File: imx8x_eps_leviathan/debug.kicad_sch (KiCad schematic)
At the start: 78 parts, among them J11 Conn_01x05_Pin, U19 CAT93C66VI-GT3, U20 FT2232HL, U21 LP38693MP-ADJ/NOPB, U22 TXS0101DCKR, U23 TXS0101DCKR, Y1 12MHz

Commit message: Did stufffffff
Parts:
- C61, C62, C63, C64, C65, C66, C67, C68, C69, C70, C71, C72, C73, C74, C75, C76, C77, C78, C79, C80, C81: footprint (none) -> EPS:C0402
- J11: footprint (none) -> Connector_PinHeader_1.00mm:PinHeader_1x05_P1.00mm_Horizontal
- L4, L5: footprint (none) -> imx8_carrier_board_footprints:L0805
- R102, R103, R104, R105, R106, R107, R108, R109, R110, R111, R112, R113, R114, R115, R116, R117, R118, R119, R120, R121, R122, R123, R124, R125, R126, R127, R128, R129, R130, R131, R132, R133, R134, R135, R136, R137, R138, R139, R140, R141, R142, R143, R144, R145, R146, R147: footprint (none) -> EPS:R0402
- USB1: footprint libs:MICRO-USB-SMD_10118194-0001LF -> imx8_carrier_board_footprints:MICRO-USB-SMD_10118194-0001LF
- Y1: footprint (none) -> imx8_carrier_board_footprints:CRYSTAL-SMD_4P-L3.2-W2.5-BL

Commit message: for john
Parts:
- R103: now not fitted
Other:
- note added: "UART Level Shifters"
- note removed: "UART Level ShifterS"
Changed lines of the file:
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@@
 		)
 	)
-	(text "UART Level ShifterS"
+	(text "UART Level Shifters"
 		(exclude_from_sim no)
 		(at 244.348 95.758 0)
@@
 		(in_bom yes)
 		(on_board yes)
-		(dnp no)
+		(dnp yes)
 		(property "Reference" "R103"
 			(at 45.466 87.376 0)

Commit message: bruh
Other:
- title: Debug USB - UART -> Leviathan 1-A
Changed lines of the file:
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@@
 	(paper "A4")
 	(title_block
-		(title "Debug USB - UART")
+		(title "Leviathan 1-A")
+		(date "2025-10-22")
+		(rev "1-A")
 		(company "Bronco Space Lab")
 		(comment 1 "By John Pollak & Luca Lanzillotta")

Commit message: Updated Schematic and SOM
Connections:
- net VCC_3V3_OUT renamed +3.3V_OBC_Perif
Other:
- note removed: "?"

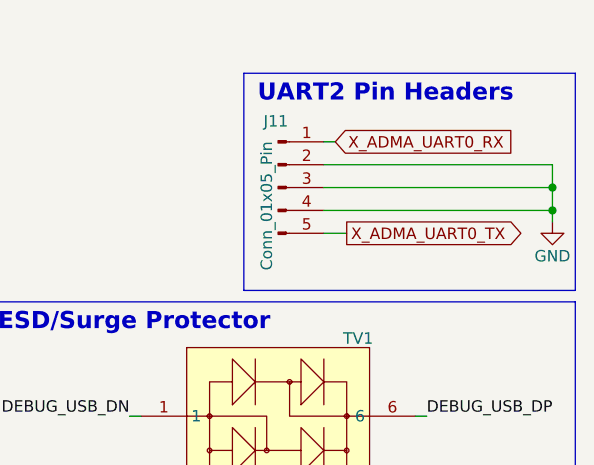
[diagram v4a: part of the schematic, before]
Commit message: Schematic Need Double Checking, But I think its done
I think ive finished adding every change we wanted to include after the merging along with all the changes requested by PHYTEC. I would like to sit down and review the muxing configuration and double check every single sheet to make sure its perfect. then we can send it off to Phytec.
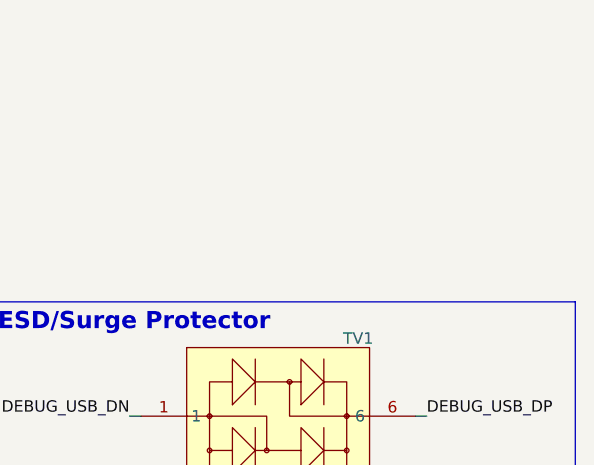
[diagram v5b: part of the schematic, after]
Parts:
- removed J11: Conn_01x05_Pin, Connector_PinHeader_1.00mm:PinHeader_1x05_P1.00mm_Horizontal, symbol Connector:Conn_01x05_Pin
- Y1: LCSC Part (none) -> C9002
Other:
- note removed: "UART2 Pin Headers"

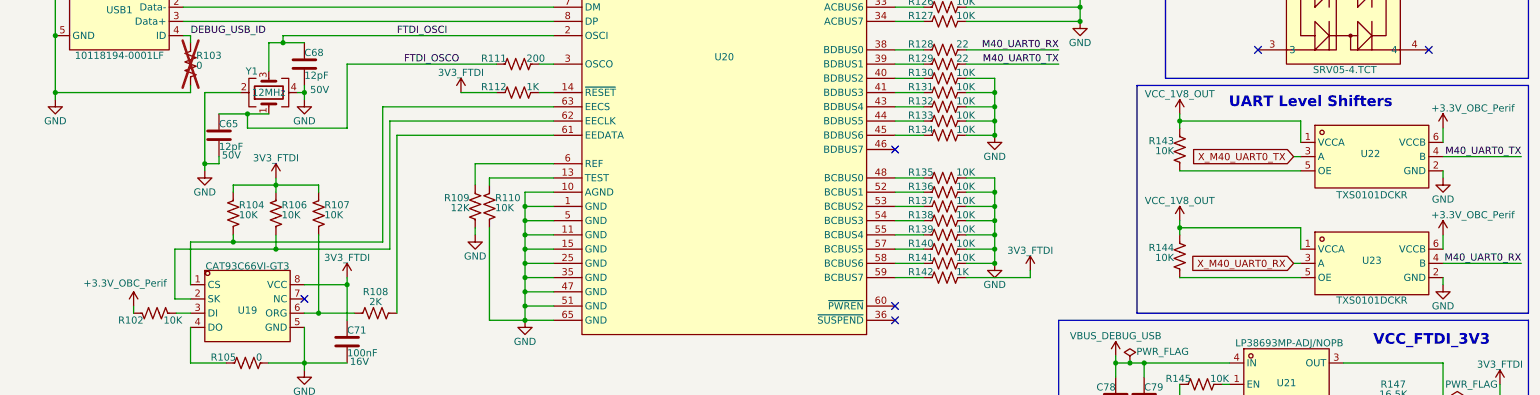
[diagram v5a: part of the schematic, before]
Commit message: Schematic Complete. Ready for Phytec.
Fixed muxing with a few things that were missing with ETH1, and corrected some missing labels. Ready for Phytecs review.
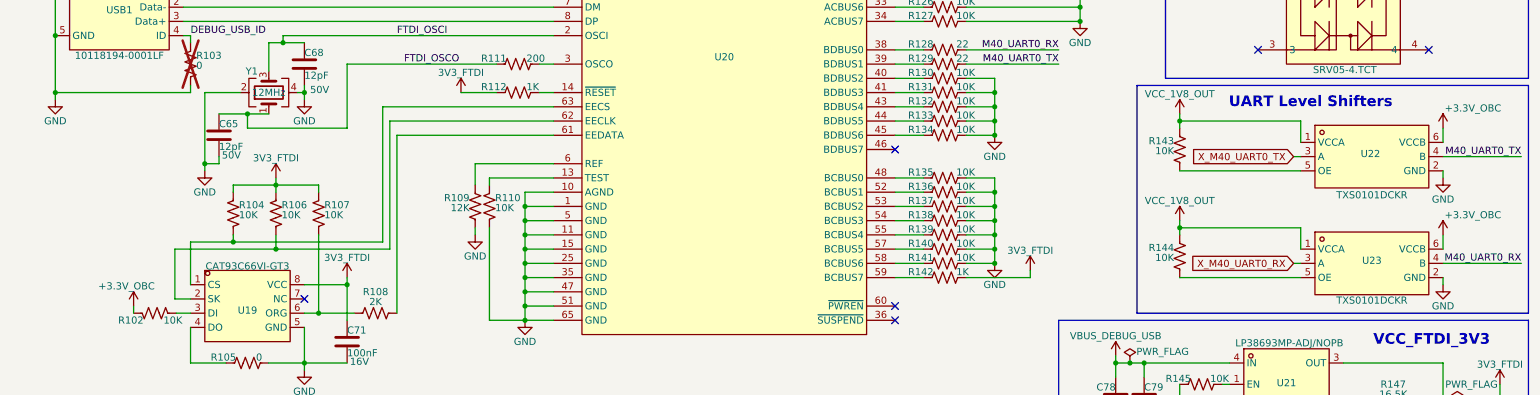
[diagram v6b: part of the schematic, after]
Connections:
- net +3.3V_OBC_Perif renamed +3.3V_OBC
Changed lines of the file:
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@@
 	)
 	(symbol
-		(lib_id "power:+3.3V")
-		(at 267.97 119.38 0)
-		(unit 1)
-		(exclude_from_sim no)
-		(in_bom yes)
-		(on_board yes)
-		(dnp no)
-		(property "Reference" "#PWR0108"
-			(at 267.97 123.19 0)
-			(effects
-				(font
-					(size 1.27 1.27)
-				)
-				(hide yes)
-			)
-		)
-		(property "Value" "+3.3V_OBC_Perif"
-			(at 273.304 115.824 0)
-			(effects
-				(font
-					(size 1.27 1.27)
-				)
-			)
-		)
-		(property "Footprint" ""
-			(at 267.97 119.38 0)
-			(effects
-				(font
-					(size 1.27 1.27)
-				)
-				(hide yes)
-			)
-		)
-		(property "Datasheet" ""
-			(at 267.97 119.38 0)
-			(effects
-				(font
-					(size 1.27 1.27)
-				)
-				(hide yes)
-			)
-		)
-		(property "Description" "Power symbol creates a global label with name \"+3.3V\""
-			(at 267.97 119.38 0)
-			(effects
-				(font
-					(size 1.27 1.27)
-				)
-				(hide yes)
-			)
-		)
-		(pin "1"
-		)
-		(instances
-			(project "imx8x_eps_leviathan"
-				(path "/bd3af9f3-19df-4a2f-8b54-98c48cea082e/1b5b2e76-614d-4307-9232-e06f7c77302d/af0dcf25-e67e-4174-8f3a-a0b953038707"
-					(reference "#PWR0108")
-					(unit 1)
-				)
-			)
-		)
-	)
-	(symbol
 		(lib_id "Device:R_US")
 		(at 179.07 116.84 270)
@@
 	(symbol
 		(lib_id "power:+3.3V")
-		(at 34.29 132.08 0)
+		(at 267.97 100.33 0)
 		(unit 1)
 		(exclude_from_sim no)
@@
 		(on_board yes)
 		(dnp no)
-		(property "Reference" "#PWR069"
-			(at 34.29 135.89 0)
+		(property "Reference" "#PWR0106"
+			(at 267.97 104.14 0)
 			(effects
 				(font
@@
 			)
 		)
-		(property "Value" "+3.3V_OBC_Perif"
-			(at 32.766 128.016 0)
+		(property "Value" "+3.3V_OBC"
+			(at 273.304 96.774 0)
 			(effects
 				(font
@@
 		)
 		(property "Footprint" ""
-			(at 34.29 132.08 0)
+			(at 267.97 100.33 0)
 			(effects
 				(font
@@
 		)
 		(property "Datasheet" ""
-			(at 34.29 132.08 0)
+			(at 267.97 100.33 0)
 			(effects
 				(font
@@
 		)
 		(property "Description" "Power symbol creates a global label with name \"+3.3V\""
-			(at 34.29 132.08 0)
+			(at 267.97 100.33 0)
 			(effects
 				(font
@@
 			(project "imx8x_eps_leviathan"
 				(path "/bd3af9f3-19df-4a2f-8b54-98c48cea082e/1b5b2e76-614d-4307-9232-e06f7c77302d/af0dcf25-e67e-4174-8f3a-a0b953038707"
-					(reference "#PWR069")
+					(reference "#PWR0106")
 					(unit 1)
 				)
@@
 	)
 	(symbol
+		(lib_id "power:+3.3V")
+		(at 34.29 132.08 0)
+		(unit 1)
+		(exclude_from_sim no)
+		(in_bom yes)
+		(on_board yes)
+		(dnp no)
+		(property "Reference" "#PWR069"
+			(at 34.29 135.89 0)
+			(effects
+				(font
+					(size 1.27 1.27)
+				)
+				(hide yes)
+			)
+		)
+		(property "Value" "+3.3V_OBC"
+			(at 33.02 128.524 0)
+			(effects
+				(font
+					(size 1.27 1.27)
+				)
+			)
+		)
+		(property "Footprint" ""
+			(at 34.29 132.08 0)
+			(effects
+				(font
+					(size 1.27 1.27)
+				)
+				(hide yes)
+			)
+		)
+		(property "Datasheet" ""
+			(at 34.29 132.08 0)
+			(effects
+				(font
+					(size 1.27 1.27)
+				)
+				(hide yes)
+			)
+		)
+		(property "Description" "Power symbol creates a global label with name \"+3.3V\""
+			(at 34.29 132.08 0)
+			(effects
+				(font
+					(size 1.27 1.27)
+				)
+				(hide yes)
+			)
+		)
+		(pin "1"
+		)
+		(instances
+			(project "imx8x_eps_leviathan"
+				(path "/bd3af9f3-19df-4a2f-8b54-98c48cea082e/1b5b2e76-614d-4307-9232-e06f7c77302d/af0dcf25-e67e-4174-8f3a-a0b953038707"
+					(reference "#PWR069")
+					(unit 1)
+				)
+			)
+		)
+	)
+	(symbol
 		(lib_id "Device:R_US")
 		(at 179.07 96.52 270)
@@
 	)
 	(symbol
+		(lib_id "power:+3.3V")
+		(at 267.97 119.38 0)
+		(unit 1)
+		(exclude_from_sim no)
+		(in_bom yes)
+		(on_board yes)
+		(dnp no)
+		(property "Reference" "#PWR0108"
+			(at 267.97 123.19 0)
+			(effects
+				(font
+					(size 1.27 1.27)
+				)
+				(hide yes)
+			)
+		)
+		(property "Value" "+3.3V_OBC"
+			(at 273.304 115.824 0)
+			(effects
+				(font
+					(size 1.27 1.27)
+				)
+			)
+		)
+		(property "Footprint" ""
+			(at 267.97 119.38 0)
+			(effects
+				(font
+					(size 1.27 1.27)
+				)
+				(hide yes)
+			)
+		)
+		(property "Datasheet" ""
+			(at 267.97 119.38 0)
+			(effects
+				(font
+					(size 1.27 1.27)
+				)
+				(hide yes)
+			)
+		)
+		(property "Description" "Power symbol creates a global label with name \"+3.3V\""
+			(at 267.97 119.38 0)
+			(effects
+				(font
+					(size 1.27 1.27)
+				)
+				(hide yes)
+			)
+		)
+		(pin "1"
+		)
+		(instances
+			(project "imx8x_eps_leviathan"
+				(path "/bd3af9f3-19df-4a2f-8b54-98c48cea082e/1b5b2e76-614d-4307-9232-e06f7c77302d/af0dcf25-e67e-4174-8f3a-a0b953038707"
+					(reference "#PWR0108")
+					(unit 1)
+				)
+			)
+		)
+	)
+	(symbol
 		(lib_id "Device:C")
 		(at 74.93 59.69 0)
@@
 					(unit 1)
 				)
-			)
-		)
-	)
-	(symbol
-		(lib_id "power:+3.3V")
-		(at 267.97 100.33 0)
-		(unit 1)
-		(exclude_from_sim no)
-		(in_bom yes)
-		(on_board yes)
-		(dnp no)
-		(property "Reference" "#PWR0106"
-			(at 267.97 104.14 0)
-			(effects
-				(font
-					(size 1.27 1.27)
-				)
-				(hide yes)
-			)
-		)
-		(property "Value" "+3.3V_OBC_Perif"
-			(at 273.304 96.774 0)
-			(effects
-				(font
-					(size 1.27 1.27)
-				)
-			)
-		)
-		(property "Footprint" ""
-			(at 267.97 100.33 0)
-			(effects
-				(font
-					(size 1.27 1.27)
-				)
-				(hide yes)
-			)
-		)
-		(property "Datasheet" ""
-			(at 267.97 100.33 0)
-			(effects
-				(font
-					(size 1.27 1.27)
-				)
-				(hide yes)
-			)
-		)
-		(property "Description" "Power symbol creates a global label with name \"+3.3V\""
-			(at 267.97 100.33 0)
-			(effects
-				(font
-					(size 1.27 1.27)
-				)
-				(hide yes)
-			)
-		)
-		(pin "1"
-		)
-		(instances
-			(project "imx8x_eps_leviathan"
-				(path "/bd3af9f3-19df-4a2f-8b54-98c48cea082e/1b5b2e76-614d-4307-9232-e06f7c77302d/af0dcf25-e67e-4174-8f3a-a0b953038707"
-					(reference "#PWR0106")
-					(unit 1)
-				)

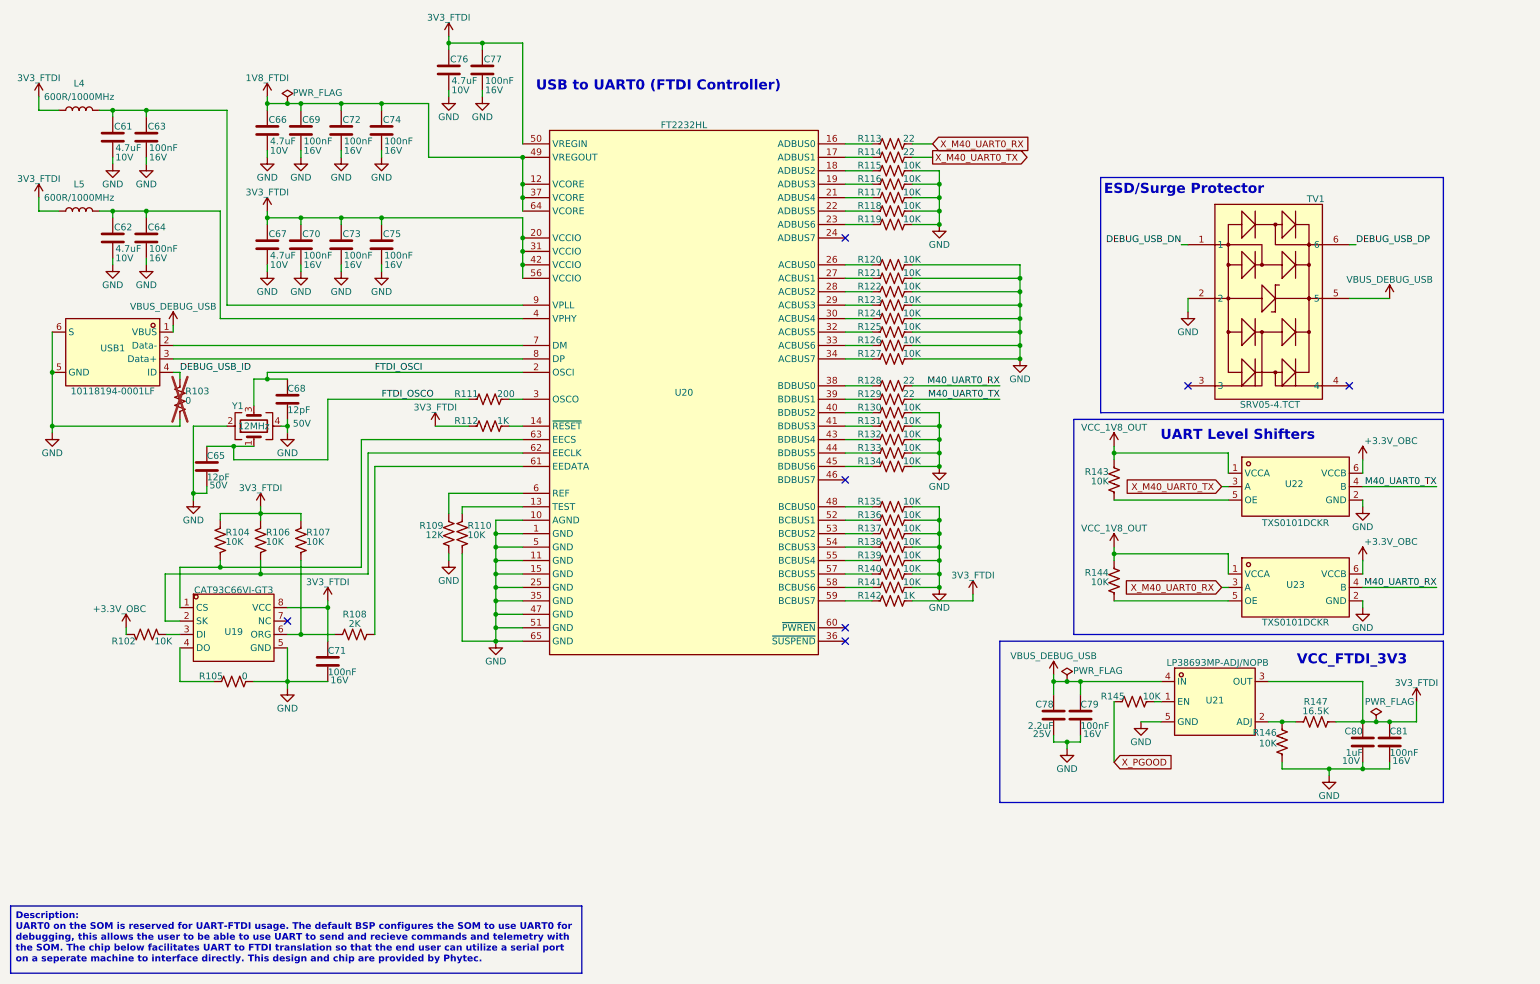
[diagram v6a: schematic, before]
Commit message: Completed Schematic, Started Layout
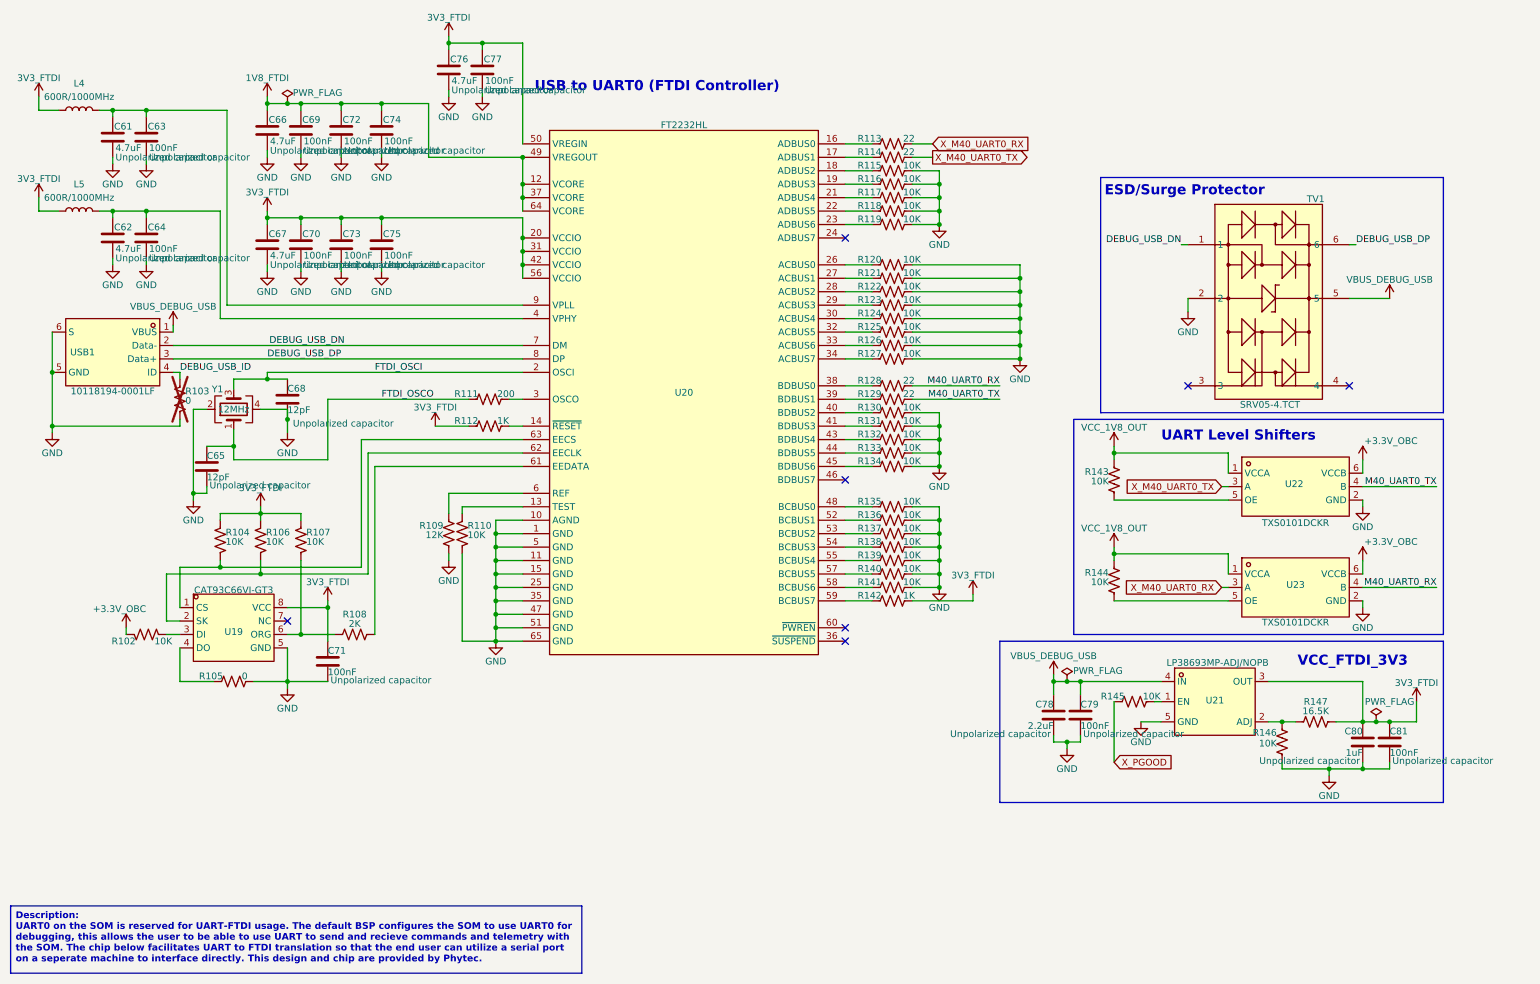
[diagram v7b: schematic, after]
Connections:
- net DEBUG_USB_DN: now also U20.7 (DM), USB1.2 (Data-)
- net DEBUG_USB_DP: now also U20.8 (DP), USB1.3 (Data+)
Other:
- moved on the sheet: Y1
